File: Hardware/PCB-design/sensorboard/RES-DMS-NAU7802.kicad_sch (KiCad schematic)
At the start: 43 parts, among them J1 Conn_01x05_Female, J2 straingauge, J3 straingauge, J4 straingauge, J5 straingauge, J6 straingauge, J7 straingauge, J8 straingauge, J9 straingauge, U1 NAU7802-SGI

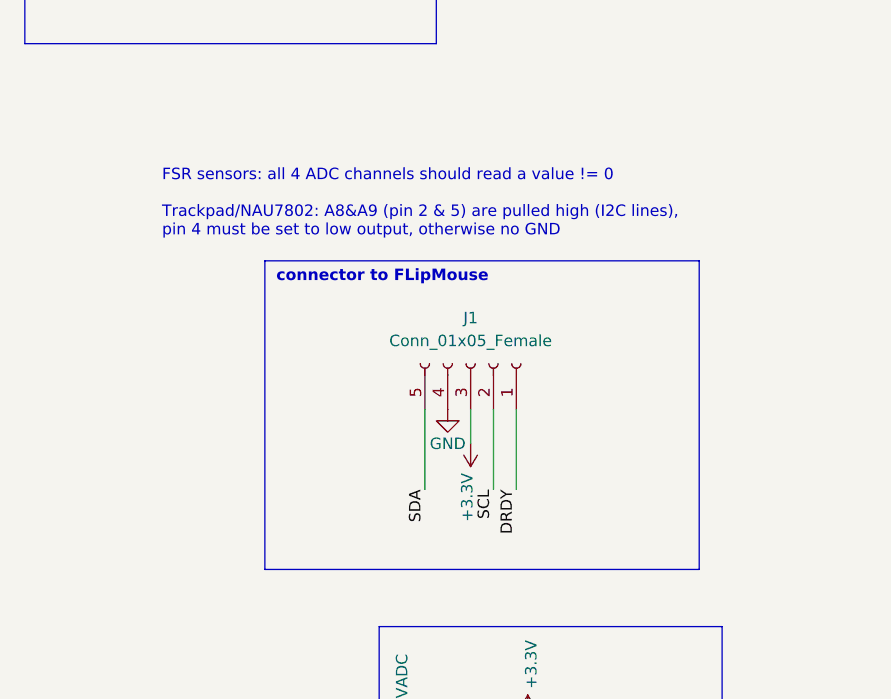
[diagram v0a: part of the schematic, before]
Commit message: Changed sensorboard connector to 6pins with 1.27mm spacing (matching the IDC cable)
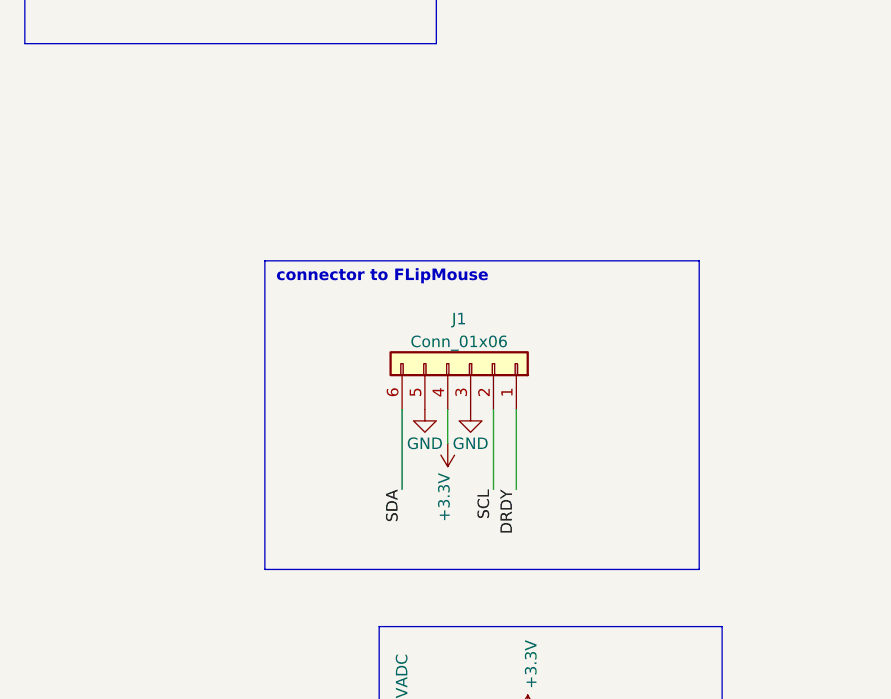
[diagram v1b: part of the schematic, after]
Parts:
- removed J1: Conn_01x05_Female, Connector_PinSocket_2.54mm:PinSocket_1x05_P2.54mm_Vertical, symbol Connector:Conn_01x05_Female
- added J1: Conn_01x06, Connector_PinHeader_1.27mm:PinHeader_1x06_P1.27mm_Vertical, symbol Connector_Generic:Conn_01x06
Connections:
- net +3.3V: now also J1.4 (Pin_4)
- net DRDY: now also J1.1 (Pin_1)
- net GND: now also J1.3 (Pin_3), J1.5 (Pin_5)
- net SCL: now also J1.2 (Pin_2)
- net SDA: now also J1.6 (Pin_6)
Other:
- note removed: "FSR sensors: all 4 ADC channels should read a value != 0 Trackpad/NAU7802: A8&A9 (pin 2 & 5) are pulled high (I2C lines), pin 4 must be set to low output, otherwise no GND"
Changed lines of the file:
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@@
     (stroke (width 0) (type default) (color 0 0 0 0))
   )
-  (wire (pts (xy 246.38 116.84) (xy 246.38 107.95))
+  (wire (pts (xy 243.84 116.84) (xy 243.84 107.95))
     (stroke (width 0) (type default) (color 0 0 0 0))
   )
@@
     (stroke (width 0) (type default) (color 0 0 0 0))
   )
-  (wire (pts (xy 251.46 107.95) (xy 251.46 111.76))
+  (wire (pts (xy 248.92 107.95) (xy 248.92 111.76))
     (stroke (width 0) (type default) (color 0 0 0 0))
   )
@@
     (effects (font (size 2.54 2.54) (thickness 0.508) bold) (justify left bottom))
   )
-  (text "FSR sensors: all 4 ADC channels should read a value != 0\n\nTrackpad/NAU7802: A8&A9 (pin 2 & 5) are pulled high (I2C lines),\npin 4 must be set to low output, otherwise no GND"
-    (at 217.17 88.9 0)
-    (effects (font (size 1.27 1.27)) (justify left bottom))
-  )
   (text "instead of using the resistors, \nyou can solder strain gauges \n(BF350-3AA) and connect their wires \nto the connectors J2-J9"
     (at 88.9 185.42 0)
@@
     (effects (font (size 1.27 1.27)) (justify right bottom))
   )
-  (label "SDA" (at 246.38 116.84 270)
+  (label "SDA" (at 243.84 116.84 270)
     (effects (font (size 1.27 1.27)) (justify right bottom))
   )
@@
     (pin "1")
   )
-  (symbol (lib_id "power:+3.3V") (at 251.46 111.76 180) (unit 1)
-    (in_bom yes) (on_board yes)
-    (property "Reference" "#PWR011" (id 0) (at 251.46 107.95 0)
-      (effects (font (size 1.27 1.27)) hide)
-    )
-    (property "Value" "+3.3V" (id 1) (at 251.079 115.0112 90)
-      (effects (font (size 1.27 1.27)) (justify left))
-    )
-    (property "Footprint" "" (id 2) (at 251.46 111.76 0)
-      (effects (font (size 1.27 1.27)) hide)
-    )
-    (property "Datasheet" "" (id 3) (at 251.46 111.76 0)
+  (symbol (lib_id "power:+3.3V") (at 248.92 111.76 180) (unit 1)
+    (in_bom yes) (on_board yes)
+    (property "Reference" "#PWR011" (id 0) (at 248.92 107.95 0)
+      (effects (font (size 1.27 1.27)) hide)
+    )
+    (property "Value" "+3.3V" (id 1) (at 248.539 115.0112 90)
+      (effects (font (size 1.27 1.27)) (justify left))
+    )
+    (property "Footprint" "" (id 2) (at 248.92 111.76 0)
+      (effects (font (size 1.27 1.27)) hide)
+    )
+    (property "Datasheet" "" (id 3) (at 248.92 111.76 0)
       (effects (font (size 1.27 1.27)) hide)
     )
@@
     (pin "2")
   )
+  (symbol (lib_id "power:GND") (at 251.46 107.95 0) (unit 1)
+    (in_bom yes) (on_board yes)
+    (property "Reference" "#PWR0103" (id 0) (at 251.46 114.3 0)
+      (effects (font (size 1.27 1.27)) hide)
+    )
+    (property "Value" "GND" (id 1) (at 251.46 111.76 0))
+    (property "Footprint" "" (id 2) (at 251.46 107.95 0)
+      (effects (font (size 1.27 1.27)) hide)
+    )
+    (property "Datasheet" "" (id 3) (at 251.46 107.95 0)
+      (effects (font (size 1.27 1.27)) hide)
+    )
+    (pin "1")
+  )
   (symbol (lib_id "Connector:TestPoint") (at 181.61 149.86 0) (unit 1)
     (in_bom yes) (on_board yes) (fields_autoplaced)
@@
     (pin "2")
   )
+  (symbol (lib_id "Connector_Generic:Conn_01x06") (at 251.46 102.87 270) (mirror x) (unit 1)
+    (in_bom yes) (on_board yes) (fields_autoplaced)
+    (property "Reference" "J1" (id 0) (at 250.19 97.9002 90))
+    (property "Value" "Conn_01x06" (id 1) (at 250.19 100.4371 90))
+    (property "Footprint" "Connector_PinHeader_1.27mm:PinHeader_1x06_P1.27mm_Vertical" (id 2) (at 251.46 102.87 0)
+      (effects (font (size 1.27 1.27)) hide)
+    )
+    (property "Datasheet" "~" (id 3) (at 251.46 102.87 0)
+      (effects (font (size 1.27 1.27)) hide)
+    )
+    (pin "1")
+    (pin "2")
+    (pin "3")
+    (pin "4")
+    (pin "5")
+    (pin "6")
+  )
   (symbol (lib_id "power:GND") (at 91.44 95.25 0) (unit 1)
     (in_bom yes) (on_board yes)
@@
     (pin "1")
     (pin "2")
-  )
-  (symbol (lib_id "Connector:Conn_01x05_Female") (at 251.46 102.87 270) (mirror x) (unit 1)
-    (in_bom yes) (on_board yes) (fields_autoplaced)
-    (property "Reference" "J1" (id 0) (at 251.46 97.79 90))
-    (property "Value" "Conn_01x05_Female" (id 1) (at 251.46 100.33 90))
-    (property "Footprint" "Connector_PinSocket_2.54mm:PinSocket_1x05_P2.54mm_Vertical" (id 2) (at 251.46 102.87 0)
-      (effects (font (size 1.27 1.27)) hide)
-    )
-    (property "Datasheet" "~" (id 3) (at 251.46 102.87 0)
-      (effects (font (size 1.27 1.27)) hide)
-    )
-    (pin "1")
-    (pin "2")
-    (pin "3")
-    (pin "4")
-    (pin "5")
   )
   (symbol (lib_id "power:PWR_FLAG") (at 257.81 156.21 0) (unit 1)
@@
     (pin "9")
   )
-  (symbol (lib_id "power:GND") (at 248.92 107.95 0) (unit 1)
-    (in_bom yes) (on_board yes)
-    (property "Reference" "#PWR0102" (id 0) (at 248.92 114.3 0)
-      (effects (font (size 1.27 1.27)) hide)
-    )
-    (property "Value" "GND" (id 1) (at 248.92 111.76 0))
-    (property "Footprint" "" (id 2) (at 248.92 107.95 0)
-      (effects (font (size 1.27 1.27)) hide)
-    )
-    (property "Datasheet" "" (id 3) (at 248.92 107.95 0)
+  (symbol (lib_id "power:GND") (at 246.38 107.95 0) (unit 1)
+    (in_bom yes) (on_board yes)
+    (property "Reference" "#PWR0102" (id 0) (at 246.38 114.3 0)
+      (effects (font (size 1.27 1.27)) hide)
+    )
+    (property "Value" "GND" (id 1) (at 246.38 111.76 0))
+    (property "Footprint" "" (id 2) (at 246.38 107.95 0)
+      (effects (font (size 1.27 1.27)) hide)
+    )
+    (property "Datasheet" "" (id 3) (at 246.38 107.95 0)
       (effects (font (size 1.27 1.27)) hide)
     )
@@
       (reference "#PWR0102") (unit 1) (value "GND") (footprint "")
     )
+    (path "/477dc908-97aa-49f1-ba19-0084f8d85b5b"
+      (reference "#PWR0103") (unit 1) (value "GND") (footprint "")
+    )
     (path "/00000000-0000-0000-0000-000061aaad58"
       (reference "C1") (unit 1) (value "1uF") (footprint "Capacitor_SMD:C_0603_1608Metric_Pad1.08x0.95mm_HandSolder")
@@
       (reference "H3") (unit 1) (value "MountingHole") (footprint "MountingHole:MountingHole_2.2mm_M2_DIN965")
     )
-    (path "/c5045078-56eb-4804-9701-71177f757880"
-      (reference "J1") (unit 1) (value "Conn_01x05_Female") (footprint "Connector_PinSocket_2.54mm:PinSocket_1x05_P2.54mm_Vertical")
+    (path "/b9eeb124-7c63-43aa-82cd-c6b9bed681d4"
+      (reference "J1") (unit 1) (value "Conn_01x06") (footprint "Connector_PinHeader_1.27mm:PinHeader_1x06_P1.27mm_Vertical")
     )
     (path "/d2d6f42d-6f79-4594-8d49-4a5dc68ffec5"

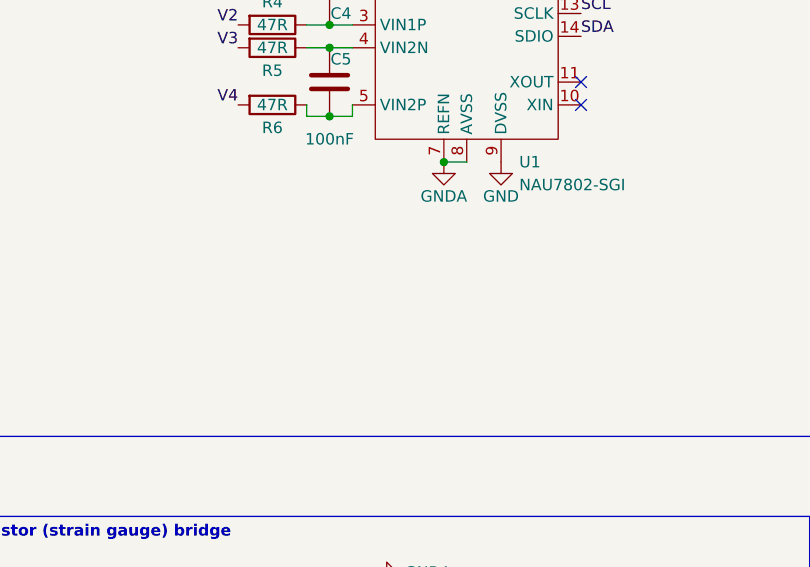
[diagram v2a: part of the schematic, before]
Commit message: Added note on input filter cutoff frequency (TBA: should we use a 10Hz filter?)
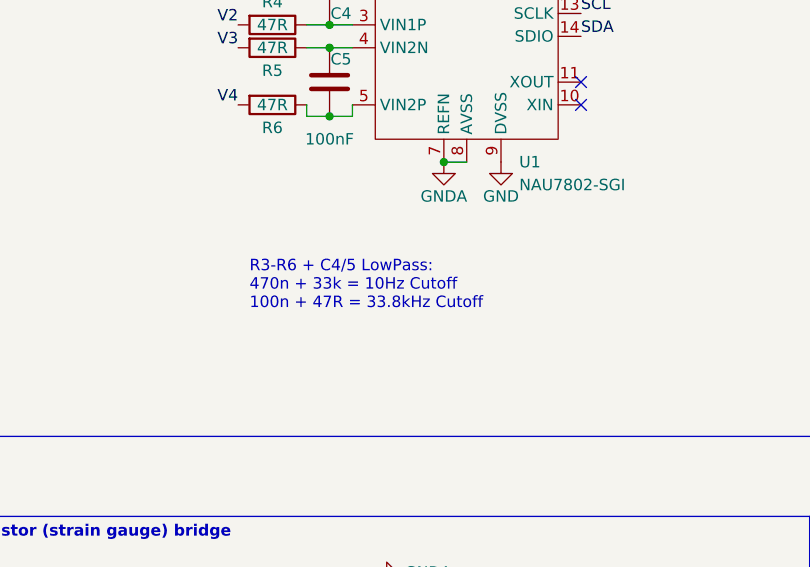
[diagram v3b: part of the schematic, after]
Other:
- note added: "R3-R6 + C4/5 LowPass: 470n + 33k = 10Hz Cutoff 100n + 47R = 33.8kHz Cutoff"
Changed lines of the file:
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@@
+    (effects (font (size 1.27 1.27)) (justify left bottom))
+  )
+  (text "R3-R6 + C4/5 LowPass:\n470n + 33k = 10Hz Cutoff\n100n + 47R = 33.8kHz Cutoff"
+    (at 63.5 111.76 0)
     (effects (font (size 1.27 1.27)) (justify left bottom))
   )

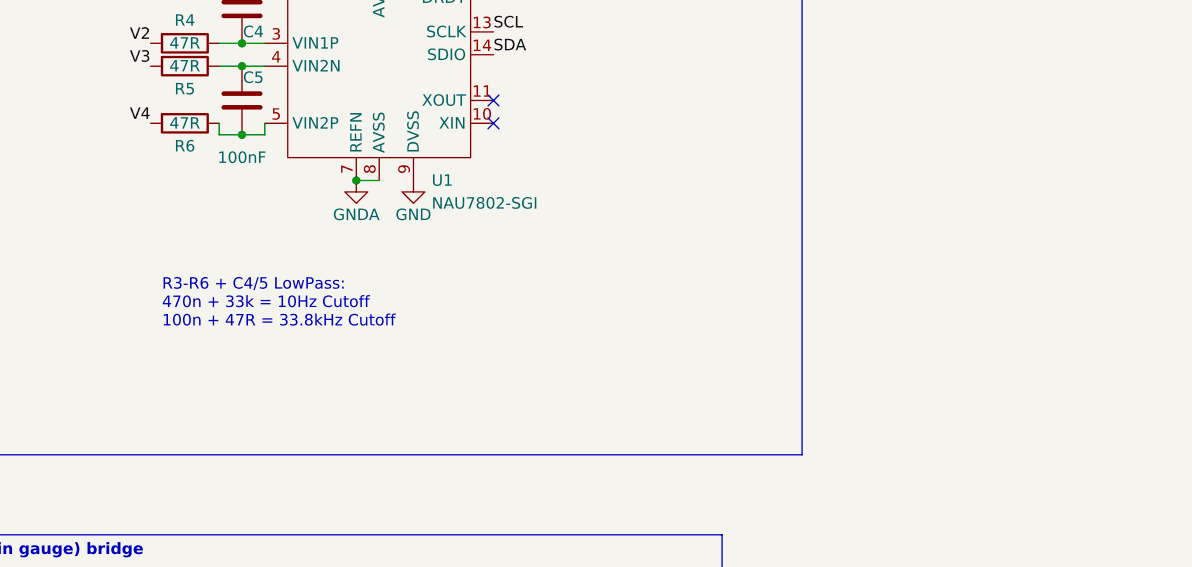
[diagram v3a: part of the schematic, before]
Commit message: Added note on filter
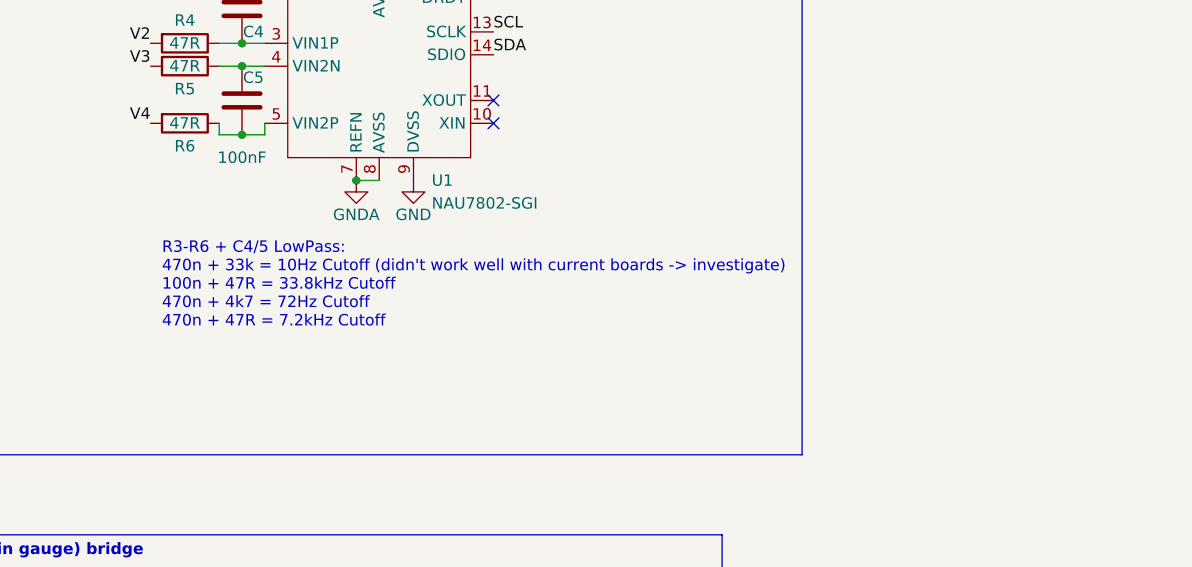
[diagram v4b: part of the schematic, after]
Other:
- note added: "R3-R6 + C4/5 LowPass: 470n + 33k = 10Hz Cutoff (didn't work well with current boards -> investigate) 100n + 47R = 33.8kHz Cutoff 470n + 4k7 = 72Hz Cutoff 470n + 47R = 7.2kHz Cutoff"
- note removed: "R3-R6 + C4/5 LowPass: 470n + 33k = 10Hz Cutoff 100n + 47R = 33.8kHz Cutoff"
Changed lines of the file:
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@@
     (effects (font (size 1.27 1.27)) (justify left bottom))
   )
-  (text "R3-R6 + C4/5 LowPass:\n470n + 33k = 10Hz Cutoff\n100n + 47R = 33.8kHz Cutoff"
+  (text "R3-R6 + C4/5 LowPass:\n470n + 33k = 10Hz Cutoff (didn't work well with current boards -> investigate)\n100n + 47R = 33.8kHz Cutoff\n470n + 4k7 = 72Hz Cutoff\n470n + 47R = 7.2kHz Cutoff"
     (at 63.5 111.76 0)
     (effects (font (size 1.27 1.27)) (justify left bottom))
